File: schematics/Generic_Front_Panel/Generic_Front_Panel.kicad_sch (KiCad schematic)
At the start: 9 parts, among them J1 Interface

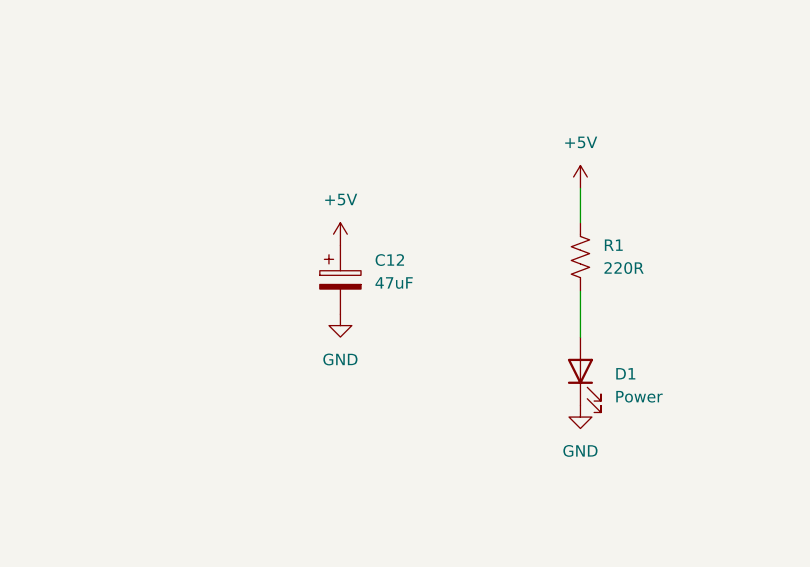
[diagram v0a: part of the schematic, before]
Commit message: Update filter capacitor to 100uF
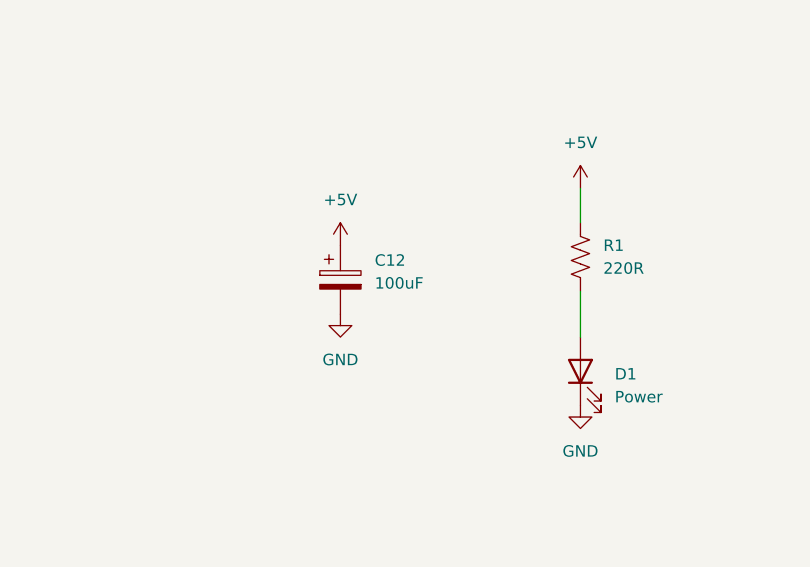
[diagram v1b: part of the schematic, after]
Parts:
- C12: value 47uF -> 100uF
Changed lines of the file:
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@@
 			)
 		)
-		(property "Value" "47uF"
+		(property "Value" "100uF"
 			(at 118.11 96.9009 0)
 			(effects
